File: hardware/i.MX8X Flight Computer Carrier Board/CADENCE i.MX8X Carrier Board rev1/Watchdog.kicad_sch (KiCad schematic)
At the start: 31 parts, among them J12 Conn_01x02, U15 TLV1704

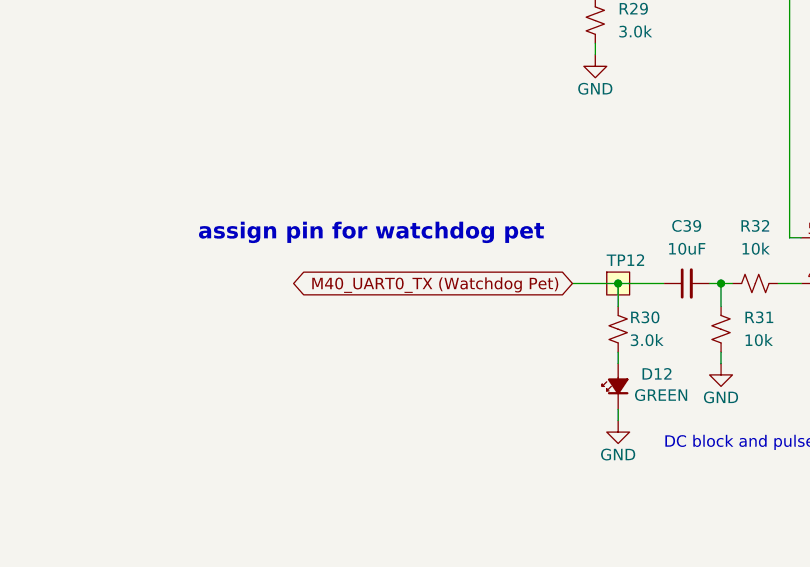
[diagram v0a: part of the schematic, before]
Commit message: i2c onboard connection reorg, updated connection list,
also slight update to board connections.
prelim adcs board connection done, ebyte, satnogs, eps
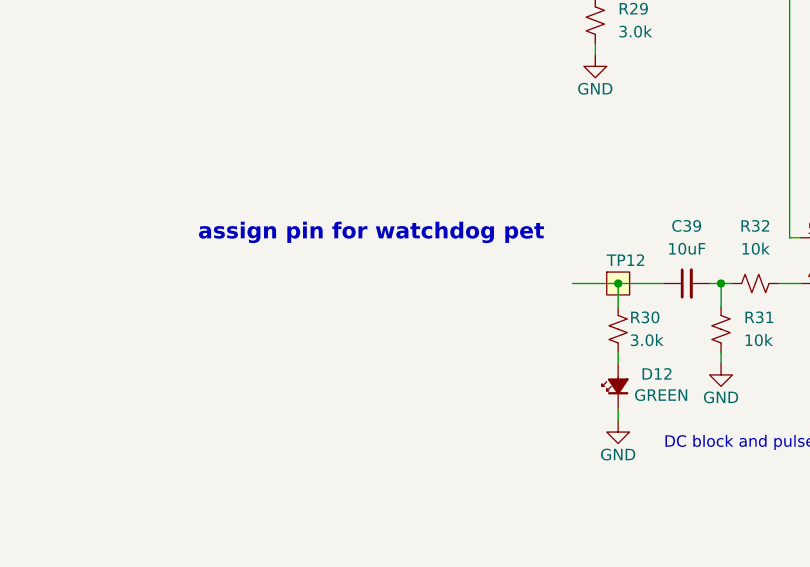
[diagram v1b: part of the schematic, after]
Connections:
- net M40_UART0_TX (Watchdog Pet): no longer names the net of C39.1, R30.1, TP12.1
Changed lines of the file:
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@@
-		)
-	)
-	(global_label "M40_UART0_TX (Watchdog Pet)"
-		(shape bidirectional)
-		(at 86.36 118.11 180)
-		(effects
-			(font
-				(size 1.27 1.27)
-			)
-			(justify right)
-		)
-		(property "Intersheetrefs" "${INTERSHEET_REFS}"
-			(at 86.36 118.11 0)
-			(effects
-				(font
-					(size 1.27 1.27)
-				)
-				(hide yes)
-			)
 		)
 	)

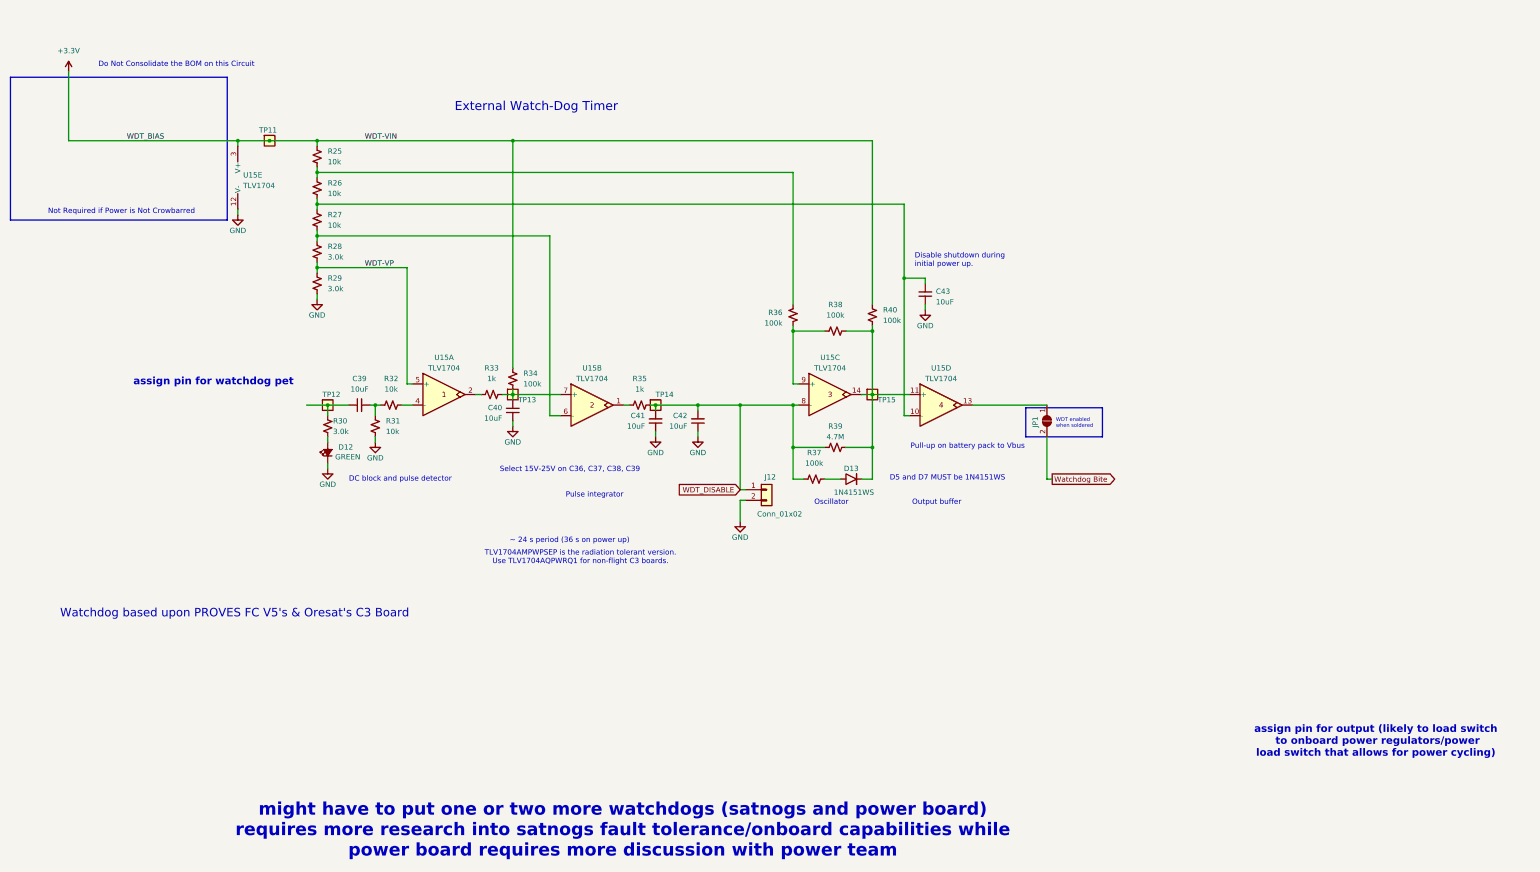
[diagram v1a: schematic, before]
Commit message: updated connections
-reset button
- fixed boot mode select
- i2c reorg/fixes
-added satnogs power monitor
-heater trigger connection (2gpio)
-more additions/fixes
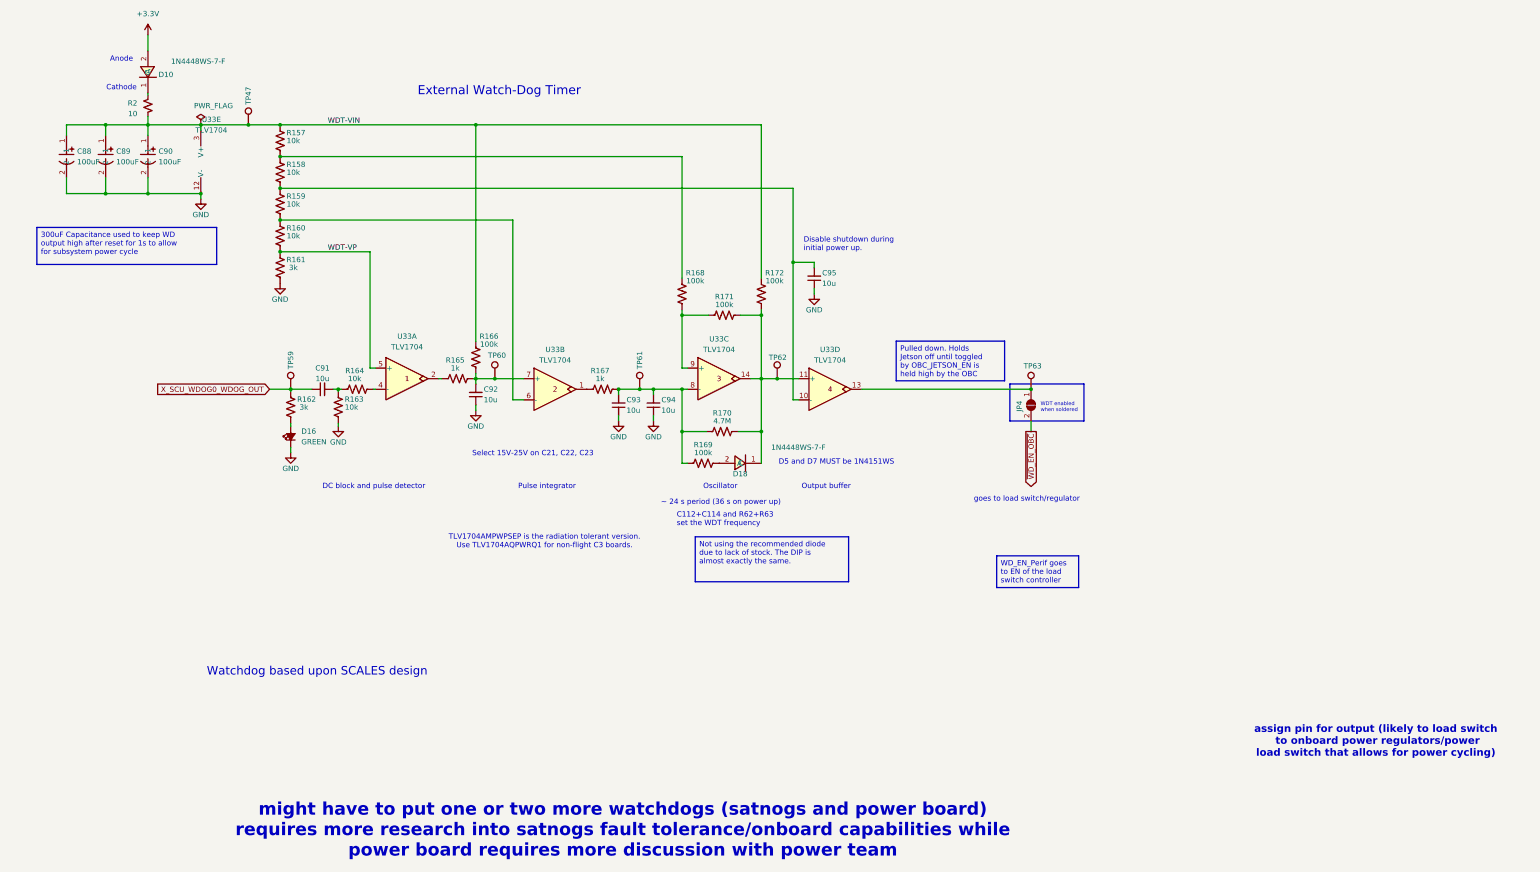
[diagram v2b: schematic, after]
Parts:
- removed C39, C40, C41, C42, C43: 10uF, Capacitor_SMD:C_0603_1608Metric, symbol Device:C_Small
- removed D12: GREEN, LED_SMD:LED_0603_1608Metric, symbol Device:LED_Small_Filled
- removed D13: 1N4151WS, Diode_SMD:D_SOD-323, symbol oresat-diodes:1N4151WS-HE3
- removed J12: Conn_01x02, Connector_PinHeader_2.54mm:PinHeader_1x02_P2.54mm_Vertical, symbol Connector_Generic:Conn_01x02
- removed JP1: SolderJumper_2_Open, Jumper:SolderJumper-2_P1.3mm_Open_RoundedPad1.0x1.5mm, symbol Jumper:SolderJumper_2_Open
- removed R25, R26, R27, R31, R32: 10k, Resistor_SMD:R_0603_1608Metric, symbol Device:R_Small_US
- removed R28, R29, R30: 3.0k, Resistor_SMD:R_0603_1608Metric, symbol Device:R_Small_US
- removed R33, R35: 1k, Resistor_SMD:R_0603_1608Metric, symbol Device:R_Small_US
- removed R34, R36, R37, R38, R40: 100k, Resistor_SMD:R_0603_1608Metric, symbol Device:R_Small_US
- removed R39: 4.7M, Resistor_SMD:R_0603_1608Metric, symbol Device:R_Small_US
- removed TP11, TP12, TP13, TP14, TP15: TestPoint-MinTH, oresat-misc:TestPoint-0.75mm-th, symbol oresat-misc:Test-Point-0.75mm-th
- removed U15: TLV1704, Package_SO:TSSOP-14_4.4x5mm_P0.65mm, symbol oresat-ics:TLV1704AIPWR
- added C88, C89, C90: 100uF, EPS:CAP-SMD_L7.3-W6.1_TCN4227M025R0100, symbol EPS:TCN4107M035R0100E
- added C91, C92, C93, C94, C95: 10u, EPS:C0402, symbol Device:C_Small
- added D10, D18: 1N4448WS-7-F, EPS:SOD-323_L1.8-W1.3-LS2.5-RD, symbol EPS:1N4448WS-7-F
- added D16: GREEN, LED_SMD:LED_0603_1608Metric, symbol Device:LED_Small_Filled
- added JP4: SolderJumper_2_Open, Jumper:SolderJumper-2_P1.3mm_Open_RoundedPad1.0x1.5mm, symbol Jumper:SolderJumper_2_Open
- added R157, R158, R159, R160, R163, R164: 10k, EPS:R0402, symbol Device:R_US
- added R161, R162: 3k, EPS:R0402, symbol Device:R_US
- added R165, R167: 1k, EPS:R0402, symbol Device:R_US
- added R166, R168, R169, R171, R172: 100k, EPS:R0402, symbol Device:R_US
- added R170: 4.7M, EPS:R0402, symbol Device:R_US
- added R2: 10, Resistor_SMD:R_1206_3216Metric, symbol Device:R_Small_US
- added TP47, TP59, TP60, TP61, TP62, TP63: TestPoint, TestPoint:TestPoint_Pad_1.0x1.0mm, symbol EPS:TestPoint
- added U33: TLV1704, Package_SO:TSSOP-14_4.4x5mm_P0.65mm, symbol EPS:TLV1704AIPWR
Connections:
- net +3.3V: now also D10.2 (A)
- net GND: now also C88.2, C89.2, C90.2, C92.1, C93.1, C94.1, C95.1, D16.1 (K), R161.1, R163.1, U33.12 (V-)
- net WDT-VP: now also R160.1, R161.2, U33.5 (+)
- new net: C92.2, R165.1, R166.2, TP60.1, U33.7 (+)
- new net: D16.2 (A), R162.1
- new net: R164.1, U33.4 (-)
- new net: C91.2, R163.2, R164.2
- new net: C93.2, C94.2, R167.1, R169.1, R170.1, TP61.1, U33.8 (-)
- new net: R168.2, R171.1, U33.9 (+)
- new net: D18.1 (C), R170.2, R171.2, R172.2, TP62.1, U33.11 (+), U33.14
- new net: D18.2 (A), R169.2
- new net: C95.2, R158.1, R159.2, U33.10 (-)
- new net: JP4.1 (A), TP63.1, U33.13
- new net: R157.1, R158.2, R168.1
- new net: R167.2, U33.1
- new net: R159.1, R160.2, U33.6 (-)
- new net: D10.1 (C), R2.1
- new net: R165.2, U33.2
- new net WDT-VIN: C88.1, C89.1, C90.1, R157.2, R166.1, R172.1, R2.2, TP47.1, U33.3 (V+)
- new net X_SCU_WDOG0_WDOG_OUT: C91.1, R162.2, TP59.1
- new net ~{WD_EN_OBC}: JP4.2 (B)
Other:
- note added: "Anode"
- note added: "C112+C114 and R62+R63 set the WDT frequency"
- note added: "Cathode"
- note added: "Select 15V-25V on C21, C22, C23"
- note added: "Watchdog based upon SCALES design"
- note added: "goes to load switch/regulator"
- note removed: "Do Not Consolidate the BOM on this Circuit"
- note removed: "Not Required if Power is Not Crowbarred"
- note removed: "Pull-up on battery pack to Vbus"
- note removed: "Select 15V-25V on C36, C37, C38, C39"
- note removed: "Watchdog based upon PROVES FC V5's & Oresat's C3 Board"
- note removed: "assign pin for watchdog pet"

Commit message: meeting changes
-watchdog
-notes
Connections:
- net ~{WD_EN_OBC} renamed X_PMIC_WDI
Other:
- note removed: "goes to load switch/regulator"
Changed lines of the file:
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@@
-		)
-	)
-	(text "goes to load switch/regulator"
-		(exclude_from_sim no)
-		(at 259.334 140.716 0)
-		(effects
-			(font
-				(size 1.27 1.27)
-			)
 		)
 	)
@@
 		)
 	)
-	(global_label "~{WD_EN_OBC}"
+	(global_label "X_PMIC_WDI"
 		(shape output)
 		(at 260.35 124.46 270)
-		(fields_autoplaced yes)
 		(effects
 			(font
@@
 		)
 		(property "Intersheetrefs" "${INTERSHEET_REFS}"
-			(at 260.35 138.4518 90)
+			(at 260.35 124.46 90)
 			(effects
 				(font
 					(size 1.27 1.27)
 				)
-				(justify right)
 				(hide yes)
 			)

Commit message: schematic reorg
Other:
- note removed: "assign pin for output (likely to load switch to onboard power regulators/power load switch that allows for power cycling)"
- note removed: "might have to put one or two more watchdogs (satnogs and power board) requires more research into satnogs fault tolerance/onboard capabilities while power board requires more discussion with power team"
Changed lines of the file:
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@@
-		)
-	)
-	(text "might have to put one or two more watchdogs (satnogs and power board)\nrequires more research into satnogs fault tolerance/onboard capabilities while\npower board requires more discussion with power team"
-		(exclude_from_sim no)
-		(at 162.306 220.218 0)
-		(effects
-			(font
-				(size 3.048 3.048)
-				(thickness 0.6096)
-				(bold yes)
-			)
 		)
 	)
@@
 			)
 		)
-	)
-	(text "assign pin for output (likely to load switch\n to onboard power regulators/power \nload switch that allows for power cycling)"
-		(exclude_from_sim no)
-		(at 343.154 198.882 0)
-		(effects
-			(font
-				(size 1.778 1.778)
-				(thickness 0.3556)
-				(bold yes)
-			)
-		)

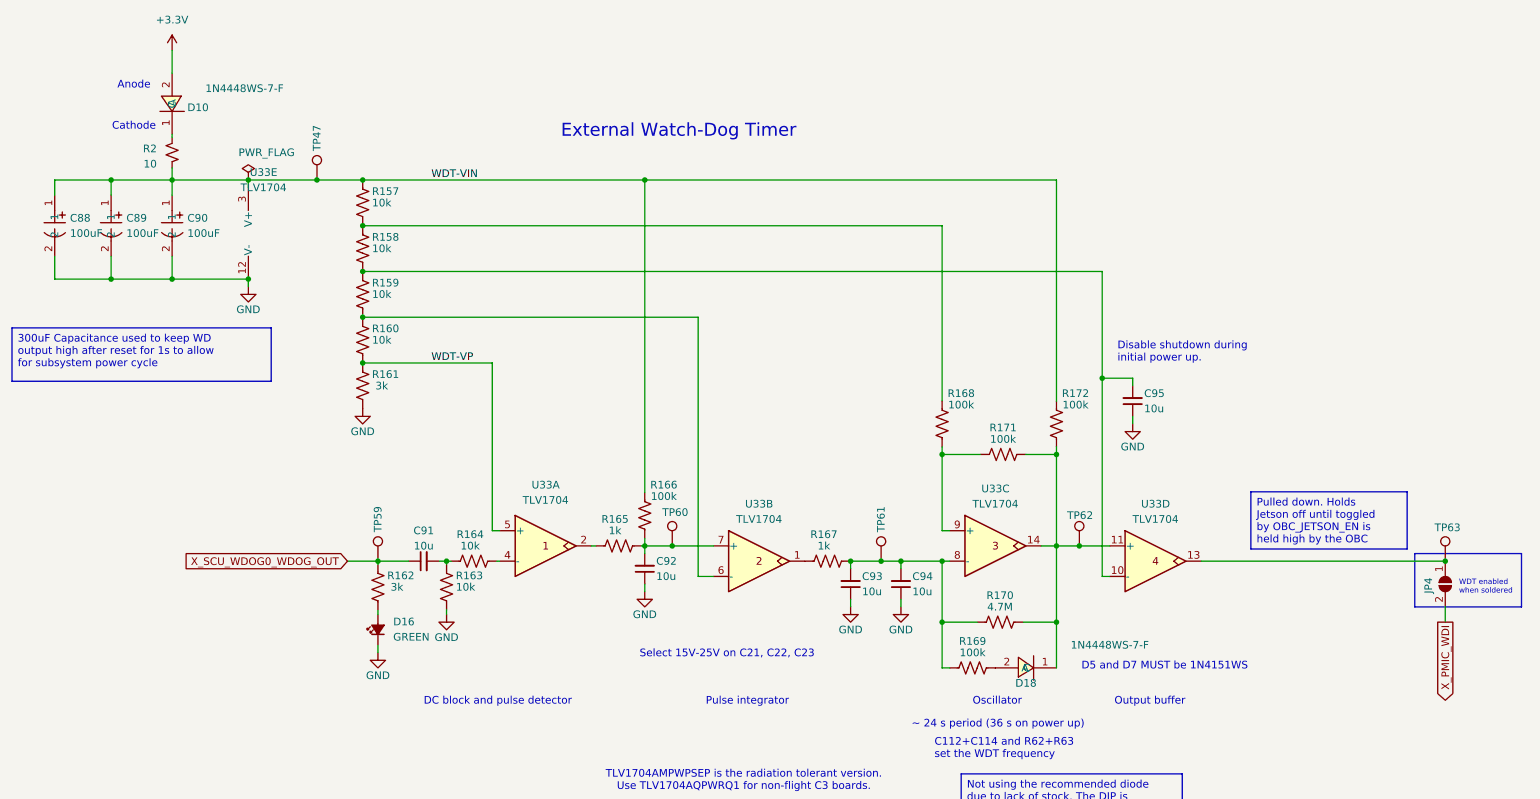
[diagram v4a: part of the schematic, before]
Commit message: added termination resistors for ebyte spi bus & fixed some erc issues
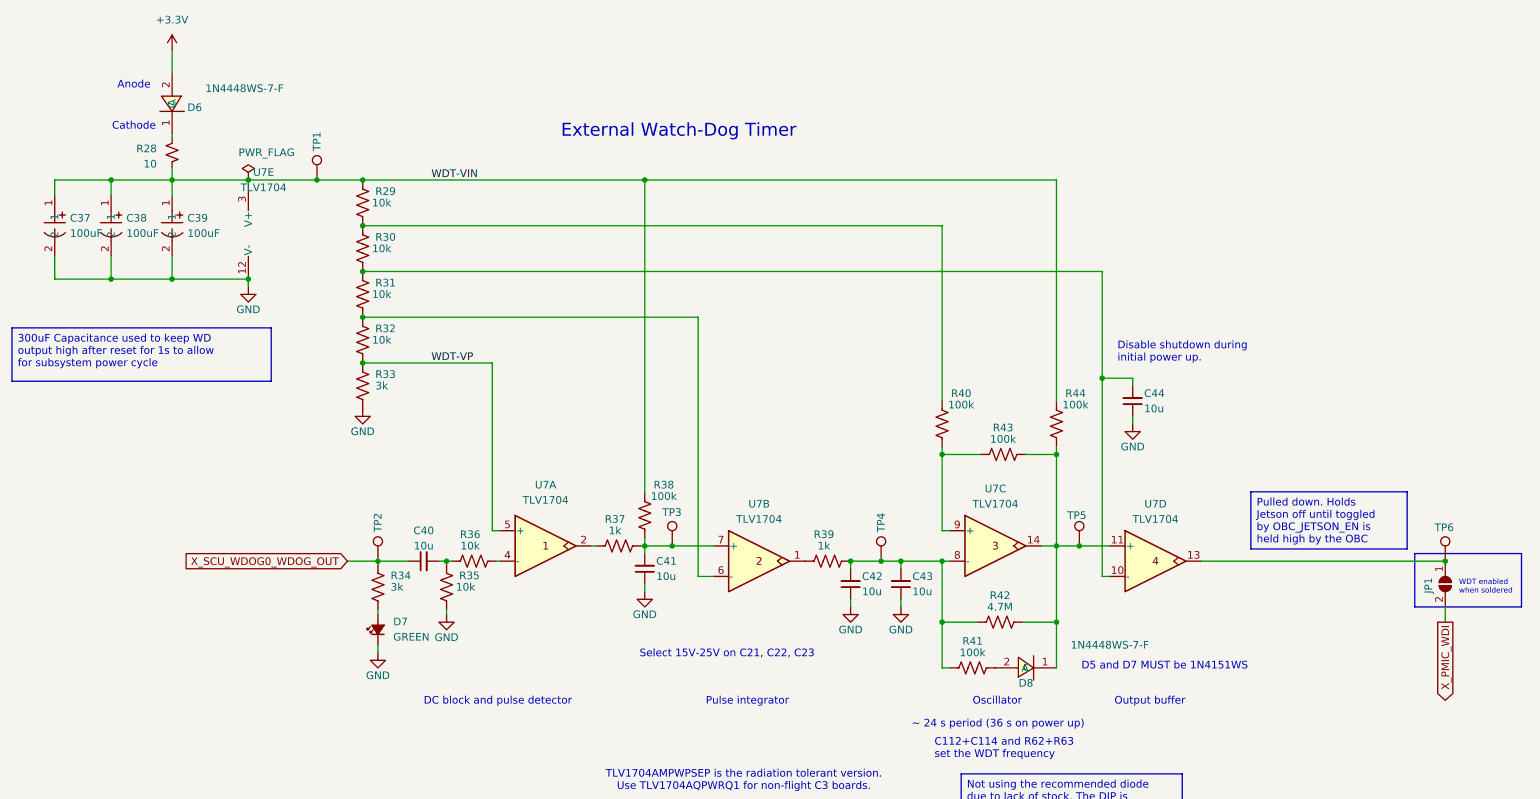
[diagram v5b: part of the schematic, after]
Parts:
- renumbered C88 to C37, C89 to C38, C90 to C39, C91 to C40, C92 to C41, C93 to C42, C94 to C43, C95 to C44, D10 to D6, D16 to D7, D18 to D8, JP4 to JP1, R2 to R28, R157 to R29, R158 to R30, R159 to R31, R160 to R32, R161 to R33, R162 to R34, R163 to R35, R164 to R36, R165 to R37, R166 to R38, R167 to R39, R168 to R40, R169 to R41, R170 to R42, R171 to R43, R172 to R44, TP47 to TP1, TP59 to TP2, TP60 to TP3, TP61 to TP4, TP62 to TP5, TP63 to TP6, U33 to U7
